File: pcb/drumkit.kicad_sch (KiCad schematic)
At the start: 26 parts, among them J1 BATTERY, J2 Conn_01x04_Female, SW1 BUTTON1, SW2 BUTTON2, SW3 BUTTON3, SW4 BUTTON4, SW5 POWER_SW, U1 Pico

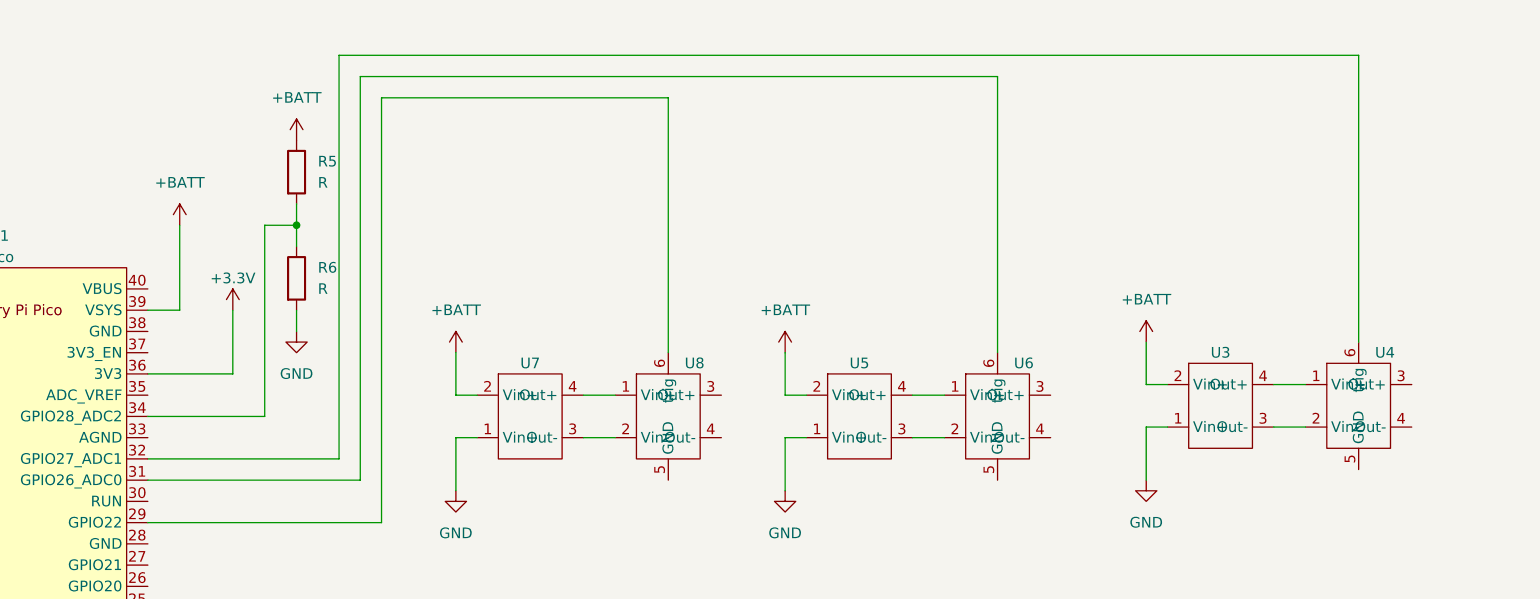
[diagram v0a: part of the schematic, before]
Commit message: squeeze in safety diodes
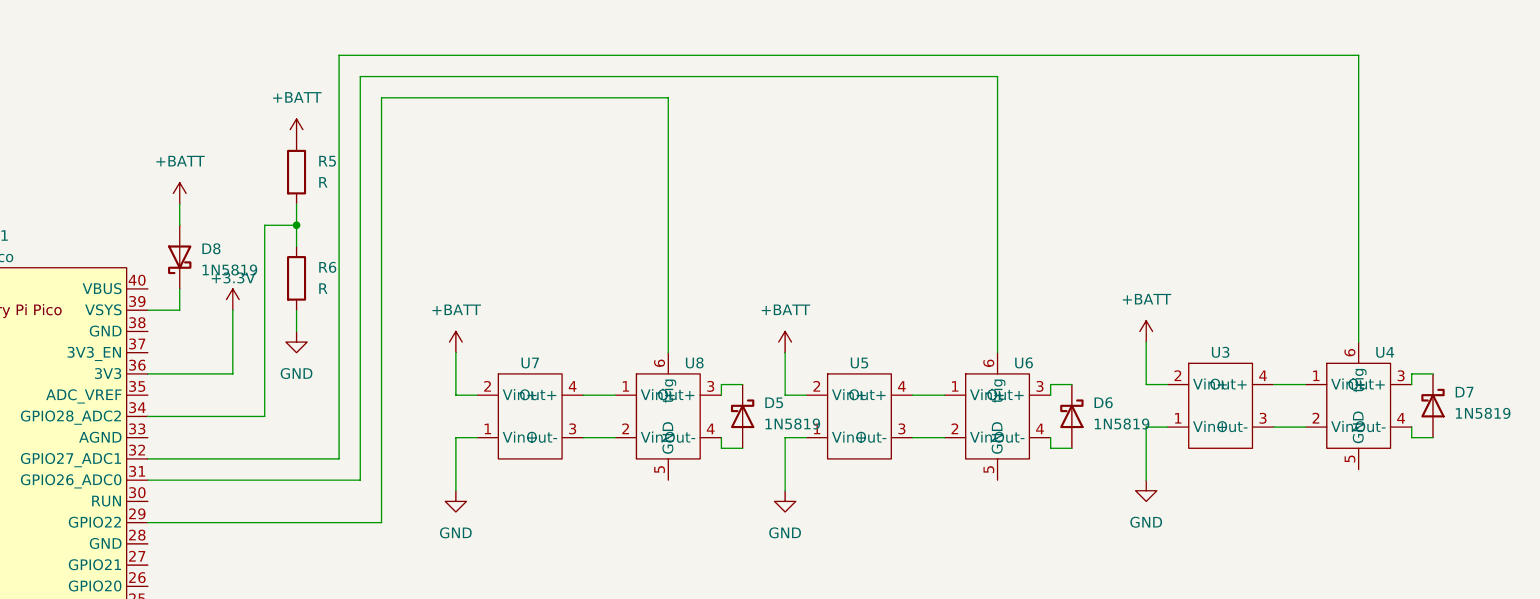
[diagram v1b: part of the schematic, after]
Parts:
- added D5, D6, D7, D8: 1N5819, Diode_THT:D_DO-41_SOD81_P10.16mm_Horizontal, symbol Diode:1N5819
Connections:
- net +BATT: now also D8.2 (A); no longer U1.39 (VSYS)
- net at U8.3 (Out+): now also D5.1 (K)
- net at U8.4 (Out-): now also D5.2 (A)
- net at U6.3 (Out+): now also D6.1 (K)
- net at U6.4 (Out-): now also D6.2 (A)
- net at U4.3 (Out+): now also D7.1 (K)
- net at U4.4 (Out-): now also D7.2 (A)
- new net: D8.1 (K), U1.39 (VSYS)
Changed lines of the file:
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@@
   (title_block
     (title "Drumkit")
-    (date "2024-03-29")
-    (rev "1.5")
+    (date "2024-03-30")
+    (rev "2")
     (comment 1 "https://git.xythobuz.de/thomas/drumkit")
     (comment 2 "Licensed under the CERN-OHL-S-2.0+")
@@
     (stroke (width 0) (type default))
   )
+  (wire (pts (xy 194.31 77.47) (xy 196.85 77.47))
+    (stroke (width 0) (type default))
+  )
   (wire (pts (xy 204.47 83.82) (xy 201.93 83.82))
     (stroke (width 0) (type default))
@@
     (stroke (width 0) (type default))
   )
+  (wire (pts (xy 276.86 82.55) (xy 276.86 83.82))
+    (stroke (width 0) (type default))
+  )
   (wire (pts (xy 27.94 182.88) (xy 27.94 185.42))
     (stroke (width 0) (type default))
@@
     (stroke (width 0) (type default))
   )
+  (wire (pts (xy 276.86 83.82) (xy 279.4 83.82))
+    (stroke (width 0) (type default))
+  )
   (wire (pts (xy 81.28 68.58) (xy 90.17 68.58))
     (stroke (width 0) (type default))
@@
     (stroke (width 0) (type default))
   )
+  (wire (pts (xy 233.68 78.74) (xy 233.68 77.47))
+    (stroke (width 0) (type default))
+  )
   (wire (pts (xy 74.93 99.06) (xy 90.17 99.06))
     (stroke (width 0) (type default))
@@
     (stroke (width 0) (type default))
   )
+  (wire (pts (xy 194.31 85.09) (xy 196.85 85.09))
+    (stroke (width 0) (type default))
+  )
   (wire (pts (xy 27.94 114.3) (xy 30.48 114.3))
     (stroke (width 0) (type default))
@@
     (stroke (width 0) (type default))
   )
+  (wire (pts (xy 233.68 83.82) (xy 233.68 85.09))
+    (stroke (width 0) (type default))
+  )
   (wire (pts (xy 177.8 83.82) (xy 181.61 83.82))
     (stroke (width 0) (type default))
   )
-  (wire (pts (xy 129.54 68.58) (xy 129.54 58.42))
-    (stroke (width 0) (type default))
-  )
   (wire (pts (xy 72.39 154.94) (xy 80.01 154.94))
     (stroke (width 0) (type default))
@@
     (stroke (width 0) (type default))
   )
+  (wire (pts (xy 233.68 85.09) (xy 236.22 85.09))
+    (stroke (width 0) (type default))
+  )
   (wire (pts (xy 161.29 129.54) (xy 161.29 147.32))
     (stroke (width 0) (type default))
@@
     (stroke (width 0) (type default))
   )
+  (wire (pts (xy 276.86 76.2) (xy 279.4 76.2))
+    (stroke (width 0) (type default))
+  )
   (wire (pts (xy 72.39 182.88) (xy 72.39 180.34))
     (stroke (width 0) (type default))
@@
     (stroke (width 0) (type default))
   )
+  (wire (pts (xy 194.31 78.74) (xy 194.31 77.47))
+    (stroke (width 0) (type default))
+  )
   (wire (pts (xy 143.51 55.88) (xy 143.51 58.42))
     (stroke (width 0) (type default))
@@
     (stroke (width 0) (type default))
   )
+  (wire (pts (xy 129.54 55.88) (xy 129.54 58.42))
+    (stroke (width 0) (type default))
+  )
   (wire (pts (xy 227.33 40.64) (xy 151.13 40.64))
     (stroke (width 0) (type default))
@@
     (stroke (width 0) (type default))
   )
+  (wire (pts (xy 276.86 77.47) (xy 276.86 76.2))
+    (stroke (width 0) (type default))
+  )
   (wire (pts (xy 72.39 182.88) (xy 82.55 182.88))
     (stroke (width 0) (type default))
@@
     (stroke (width 0) (type default))
   )
+  (wire (pts (xy 129.54 66.04) (xy 129.54 68.58))
+    (stroke (width 0) (type default))
+  )
   (wire (pts (xy 125.73 93.98) (xy 153.67 93.98))
     (stroke (width 0) (type default))
   )
+  (wire (pts (xy 194.31 83.82) (xy 194.31 85.09))
+    (stroke (width 0) (type default))
+  )
   (wire (pts (xy 62.23 182.88) (xy 72.39 182.88))
     (stroke (width 0) (type default))
@@
   )
   (wire (pts (xy 26.67 27.94) (xy 31.75 27.94))
+    (stroke (width 0) (type default))
+  )
+  (wire (pts (xy 233.68 77.47) (xy 236.22 77.47))
     (stroke (width 0) (type default))
   )
@@
     )
   )
+  (symbol (lib_id "Diode:1N5819") (at 236.22 81.28 270) (unit 1)
+    (in_bom yes) (on_board yes) (dnp no) (fields_autoplaced)
+    (property "Reference" "D6" (at 238.76 79.6925 90)
+      (effects (font (size 1.27 1.27)) (justify left))
+    )
+    (property "Value" "1N5819" (at 238.76 82.2325 90)
+      (effects (font (size 1.27 1.27)) (justify left))
+    )
+    (property "Footprint" "Diode_THT:D_DO-41_SOD81_P10.16mm_Horizontal" (at 231.775 81.28 0)
+      (effects (font (size 1.27 1.27)) hide)
+    )
+    (property "Datasheet" "http://www.vishay.com/docs/88525/1n5817.pdf" (at 236.22 81.28 0)
+      (effects (font (size 1.27 1.27)) hide)
+    )
+    (pin "2")
+    (pin "1")
+    (instances
+      (project "drumkit"
+        (path "/13d14c25-8baa-4714-9b30-86acf6c3cb37"
+          (reference "D6") (unit 1)
+        )
+      )
+    )
+  )
   (symbol (lib_id "Device:LED") (at 82.55 165.1 90) (unit 1)
     (in_bom yes) (on_board yes) (dnp no) (fields_autoplaced)
@@
     )
   )
+  (symbol (lib_id "Diode:1N5819") (at 279.4 80.01 270) (unit 1)
+    (in_bom yes) (on_board yes) (dnp no) (fields_autoplaced)
+    (property "Reference" "D7" (at 281.94 78.4225 90)
+      (effects (font (size 1.27 1.27)) (justify left))
+    )
+    (property "Value" "1N5819" (at 281.94 80.9625 90)
+      (effects (font (size 1.27 1.27)) (justify left))
+    )
+    (property "Footprint" "Diode_THT:D_DO-41_SOD81_P10.16mm_Horizontal" (at 274.955 80.01 0)
+      (effects (font (size 1.27 1.27)) hide)
+    )
+    (property "Datasheet" "http://www.vishay.com/docs/88525/1n5817.pdf" (at 279.4 80.01 0)
+      (effects (font (size 1.27 1.27)) hide)
+    )
+    (pin "2")
+    (pin "1")
+    (instances
+      (project "drumkit"
+        (path "/13d14c25-8baa-4714-9b30-86acf6c3cb37"
+          (reference "D7") (unit 1)
+        )
+      )
+    )
+  )
   (symbol (lib_name "GND_1") (lib_id "power:GND") (at 245.11 88.9 0) (unit 1)
     (in_bom yes) (on_board yes) (dnp no) (fields_autoplaced)
@@
     )
   )
-  (symbol (lib_id "power:+BATT") (at 129.54 58.42 0) (unit 1)
+  (symbol (lib_id "power:+BATT") (at 129.54 55.88 0) (unit 1)
     (in_bom yes) (on_board yes) (dnp no)
-    (property "Reference" "#PWR03" (at 129.54 62.23 0)
-      (effects (font (size 1.27 1.27)) hide)
-    )
-    (property "Value" "+BATT" (at 129.54 53.34 0)
-      (effects (font (size 1.27 1.27)))
-    )
-    (property "Footprint" "" (at 129.54 58.42 0)
-      (effects (font (size 1.27 1.27)) hide)
-    )
-    (property "Datasheet" "" (at 129.54 58.42 0)
+    (property "Reference" "#PWR03" (at 129.54 59.69 0)
+      (effects (font (size 1.27 1.27)) hide)
+    )
+    (property "Value" "+BATT" (at 129.54 50.8 0)
+      (effects (font (size 1.27 1.27)))
+    )
+    (property "Footprint" "" (at 129.54 55.88 0)
+      (effects (font (size 1.27 1.27)) hide)
+    )
+    (property "Datasheet" "" (at 129.54 55.88 0)
       (effects (font (size 1.27 1.27)) hide)
     )
@@
     )
   )
+  (symbol (lib_id "Diode:1N5819") (at 196.85 81.28 270) (unit 1)
+    (in_bom yes) (on_board yes) (dnp no) (fields_autoplaced)
+    (property "Reference" "D5" (at 199.39 79.6925 90)
+      (effects (font (size 1.27 1.27)) (justify left))
+    )
+    (property "Value" "1N5819" (at 199.39 82.2325 90)
+      (effects (font (size 1.27 1.27)) (justify left))
+    )
+    (property "Footprint" "Diode_THT:D_DO-41_SOD81_P10.16mm_Horizontal" (at 192.405 81.28 0)
+      (effects (font (size 1.27 1.27)) hide)
+    )
+    (property "Datasheet" "http://www.vishay.com/docs/88525/1n5817.pdf" (at 196.85 81.28 0)
+      (effects (font (size 1.27 1.27)) hide)
+    )
+    (pin "2")
+    (pin "1")
+    (instances
+      (project "drumkit"
+        (path "/13d14c25-8baa-4714-9b30-86acf6c3cb37"
+          (reference "D5") (unit 1)
+        )
+      )
+    )
+  )
   (symbol (lib_id "dk_Encoders:PEC11R-4215F-S0024") (at 149.86 127 0) (mirror y) (unit 1)
     (in_bom yes) (on_board yes) (dnp no)
@@
         )
       )
+    )
+  )
+  (symbol (lib_id "Diode:1N5819") (at 129.54 62.23 90) (unit 1)
+    (in_bom yes) (on_board yes) (dnp no) (fields_autoplaced)
+    (property "Reference" "D8" (at 132.08 61.2775 90)
+      (effects (font (size 1.27 1.27)) (justify right))
+    )
+    (property "Value" "1N5819" (at 132.08 63.8175 90)
+      (effects (font (size 1.27 1.27)) (justify right))
+    )
+    (property "Footprint" "Diode_THT:D_DO-41_SOD81_P10.16mm_Horizontal" (at 133.985 62.23 0)
+      (effects (font (size 1.27 1.27)) hide)
+    )
+    (property "Datasheet" "http://www.vishay.com/docs/88525/1n5817.pdf" (at 129.54 62.23 0)
+      (effects (font (size 1.27 1.27)) hide)
+    )
+    (pin "2")
+    (pin "1")
+    (instances
+      (project "drumkit"
+        (path "/13d14c25-8baa-4714-9b30-86acf6c3cb37"
+          (reference "D8") (unit 1)
+        )
+      )

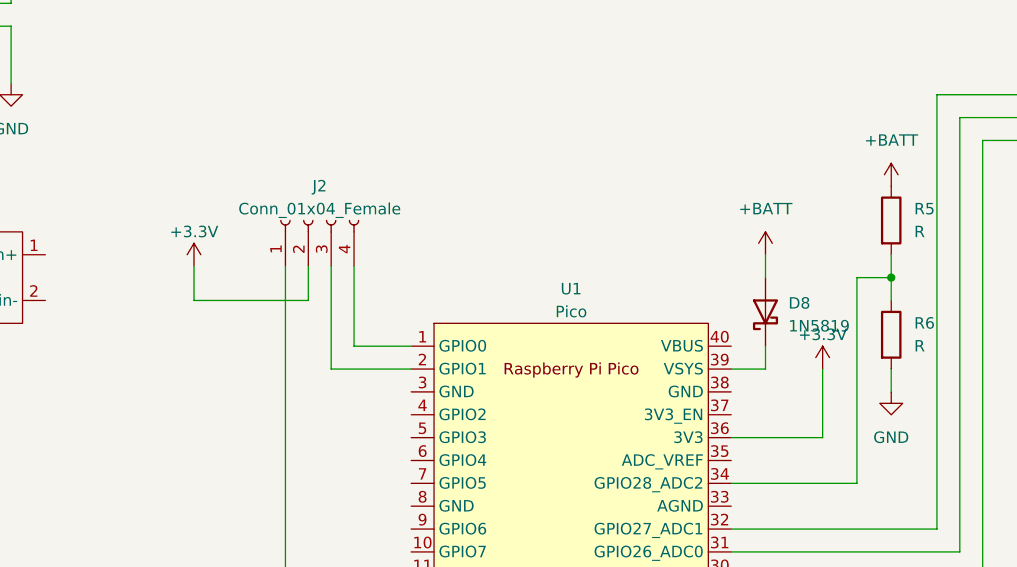
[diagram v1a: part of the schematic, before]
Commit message: add 3d model to prototype pcb
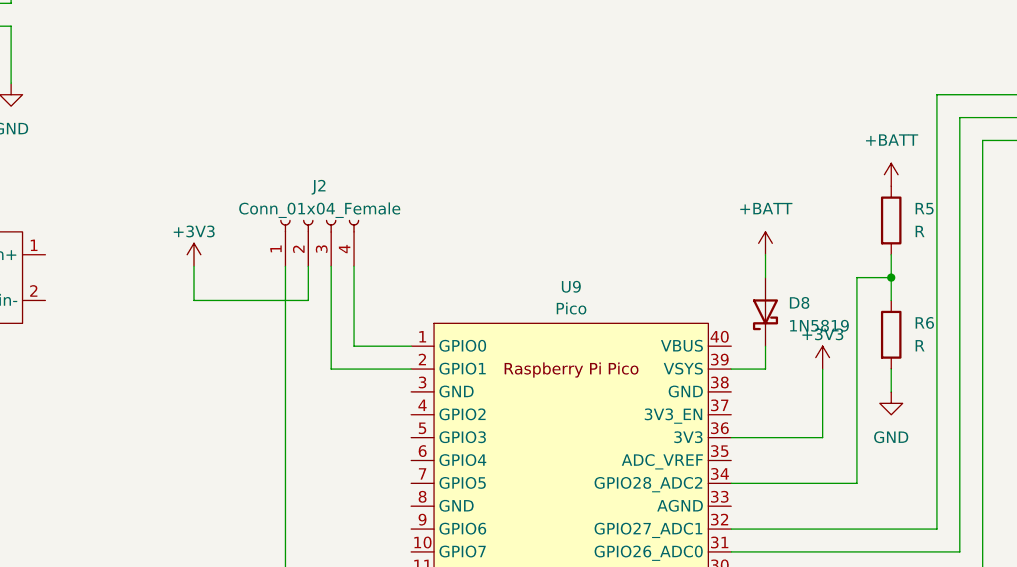
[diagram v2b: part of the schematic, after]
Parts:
- removed U1: Pico, MCU_RaspberryPi_and_Boards:RPi_Pico_SMD_TH, symbol MCU_RaspberryPi_and_Boards:Pico
- added U9: Pico, KiCad-RP-Pico:RPi_Pico_SMD_TH_noSWD, symbol KiCad-RP-Pico:Pico
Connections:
- net +3V3: now also U9.36 (3V3)
- net GND: now also U9.23 (GND)
- net at D3.2 (A): now also U9.17 (GPIO13)
- net at R5.2, R6.1: now also U9.34 (GPIO28_ADC2)
- net at U8.6 (trig): now also U9.29 (GPIO22)
- net at D4.2 (A): now also U9.20 (GPIO15)
- net at SW1.2: now also U9.11 (GPIO8)
- net at SW2.2: now also U9.12 (GPIO9)
- net at U6.6 (trig): now also U9.31 (GPIO26_ADC0)
- net at SW3.2: now also U9.16 (GPIO12)
- net at U4.6 (trig): now also U9.32 (GPIO27_ADC1)
- net at D2.2 (A): now also U9.15 (GPIO11)
- net at S1.1: now also U9.21 (GPIO16)
- net at S1.A (CH_A): now also U9.22 (GPIO17)
- net at S1.B (CH_B): now also U9.24 (GPIO18)
- net at D8.1 (K): now also U9.39 (VSYS)
- net at J2.4 (Pin_4): now also U9.1 (GPIO0)
- net at J2.1 (Pin_1): now also U9.13 (GND)
- net at D1.2 (A): now also U9.14 (GPIO10)
- net at SW4.2: now also U9.19 (GPIO14)
- net at J2.3 (Pin_3): now also U9.2 (GPIO1)
